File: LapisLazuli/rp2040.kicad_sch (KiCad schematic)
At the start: 32 parts, among them P1 USB_C_Plug_USB2.0, SW1 SW_Push, SW2 SW_Push, U10 W25Q128JVS, U11 RP2040, U9 NCP1117-3.3_SOT223, Y1 ABM8-272-T3

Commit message: Everything but I2C mux I think
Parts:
- removed U9: NCP1117-3.3_SOT223, Package_TO_SOT_SMD:SOT-223-3_TabPin2, symbol Regulator_Linear:NCP1117-3.3_SOT223
- added R19, R20: 5.1k, symbol Device:R_Small_US
- added U12: AZ1117IH-3.3TRG1, AZ1117IH-3.3TRG1:SOT230P700X185-4N, symbol AZ1117IH-3.3TRG1:AZ1117IH-3.3TRG1
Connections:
- net +3V3: now also U12.2 (OUTPUT), U12.4 (VOUT)
- net GND: now also R19.2, R20.2, U12.1 (GND)
- net USB_D+: now also P1.A6 (D+); no longer P1.A7 (D-)
- net USB_D-: now also P1.A7 (D-); no longer P1.A6 (D+)
- net VBUS: now also D1.1 (K), U12.3 (INPUT); no longer D1.2 (A)
- net at P1.A4 (VBUS), P1.A9 (VBUS), P1.B4 (VBUS)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: now also D1.2 (A); no longer D1.1 (K)
- net at P1.A5 (CC): now also R20.1
- net at P1.B5 (VCONN): now also R19.1
- net RS485_TX: now reaches U11.27 (GPIO16)
- net RS485_RX: now reaches U11.28 (GPIO17)
- net RS485_SEND: now reaches U11.29 (GPIO18)
- net I2C_SDA: now reaches U11.31 (GPIO20)
- net I2C_SCL: now reaches U11.32 (GPIO21)
- net I2C_MUX_RESET': now reaches U11.34 (GPIO22)
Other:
- moved on the sheet: C20, D1

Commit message: Most footprints and second I2C extender
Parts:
- C17, C18: footprint Capacitor_SMD:C_0402_1005Metric -> Capacitor_SMD:C_0603_1608Metric; Digikey (none) -> C1644; LCSC (none) -> C1644
- C19, C20, C33: Digikey (none) -> C19702; LCSC (none) -> C19702
- C21, C22, C23, C25, C27, C28, C29, C30, C31, C32: footprint Capacitor_SMD:C_0402_1005Metric -> Capacitor_SMD:C_0603_1608Metric; Digikey (none) -> C14663; LCSC (none) -> C14663
- C24, C26: footprint Capacitor_SMD:C_0402_1005Metric -> Capacitor_SMD:C_0603_1608Metric; Digikey (none) -> C15849; LCSC (none) -> C15849
- C34: value 0.1uF -> 100n; footprint Capacitor_SMD:C_0603_1608Metric_Pad1.08x0.95mm_HandSolder -> Capacitor_SMD:C_0603_1608Metric; Digikey (none) -> C14663; LCSC (none) -> C14663
- D1: Digikey (none) -> C191023; LCSC (none) -> C191023
- P1: footprint (none) -> Connector_USB:USB_C_Receptacle_HRO_TYPE-C-31-M-12; LCSC (none) -> C165948
- R13, R15: footprint Resistor_SMD:R_0402_1005Metric -> Resistor_SMD:R_0603_1608Metric; LCSC (none) -> C21190
- R14: footprint Resistor_SMD:R_0402_1005Metric -> Resistor_SMD:R_0603_1608Metric
- R16, R17: footprint Resistor_SMD:R_0402_1005Metric -> Resistor_SMD:R_0603_1608Metric; LCSC (none) -> C25190
- R18: footprint Resistor_SMD:R_0603_1608Metric_Pad0.98x0.95mm_HandSolder -> Resistor_SMD:R_0603_1608Metric; LCSC (none) -> C25804
- R19, R20: footprint (none) -> Resistor_SMD:R_0603_1608Metric; LCSC (none) -> C23186
- SW1, SW2: LCSC (none) -> C221784
- U10: LCSC (none) -> C97521
- U11: footprint RP2040_minimal_r2:RP2040-QFN-56 -> MCU_RaspberryPi_and_Boards:RP2040-QFN-56; Digikey (none) -> C2040; LCSC (none) -> C2040
- U12: footprint AZ1117IH-3.3TRG1:SOT230P700X185-4N -> Package_TO_SOT_SMD:SOT-223-3_TabPin2; LCSC (none) -> C108495
- Y1: Digikey (none) -> C20625731; LCSC (none) -> C20625731

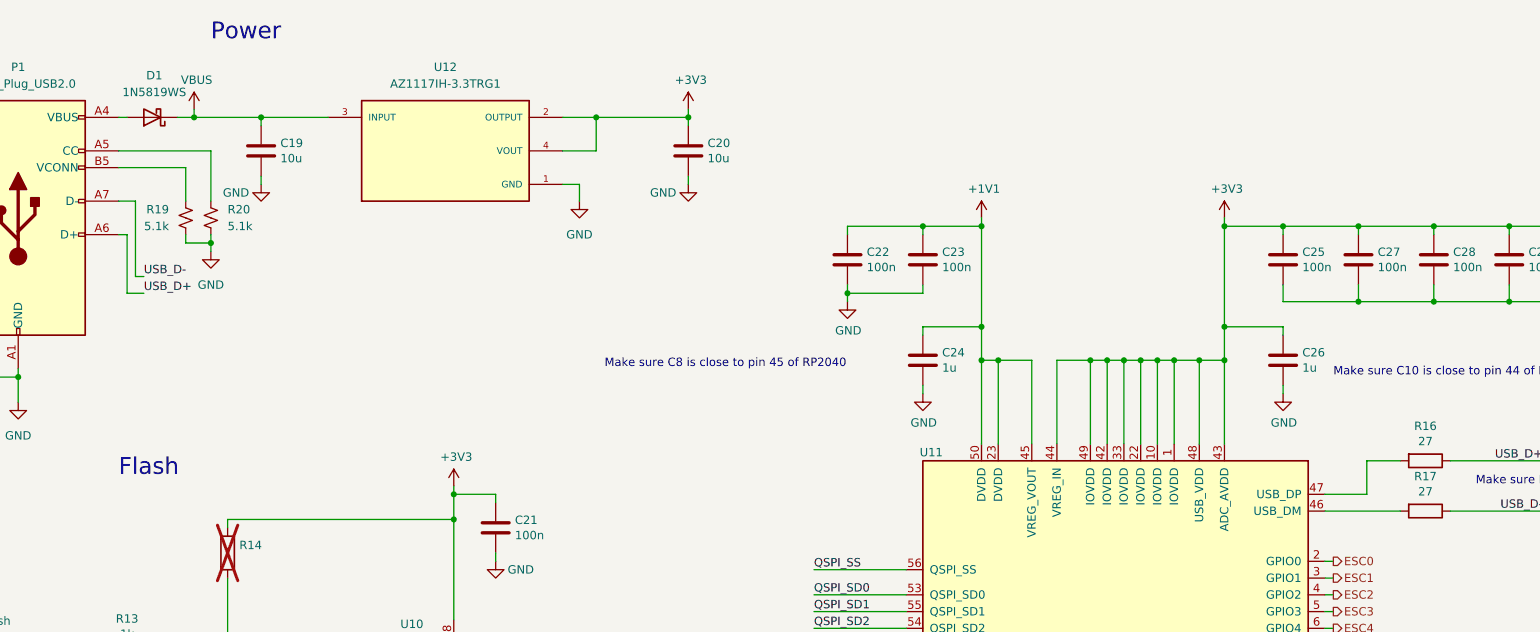
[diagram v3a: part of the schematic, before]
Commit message: Add current pcb layout
- Missing connections to power board
- Missing LEDs
- Missing Test Points
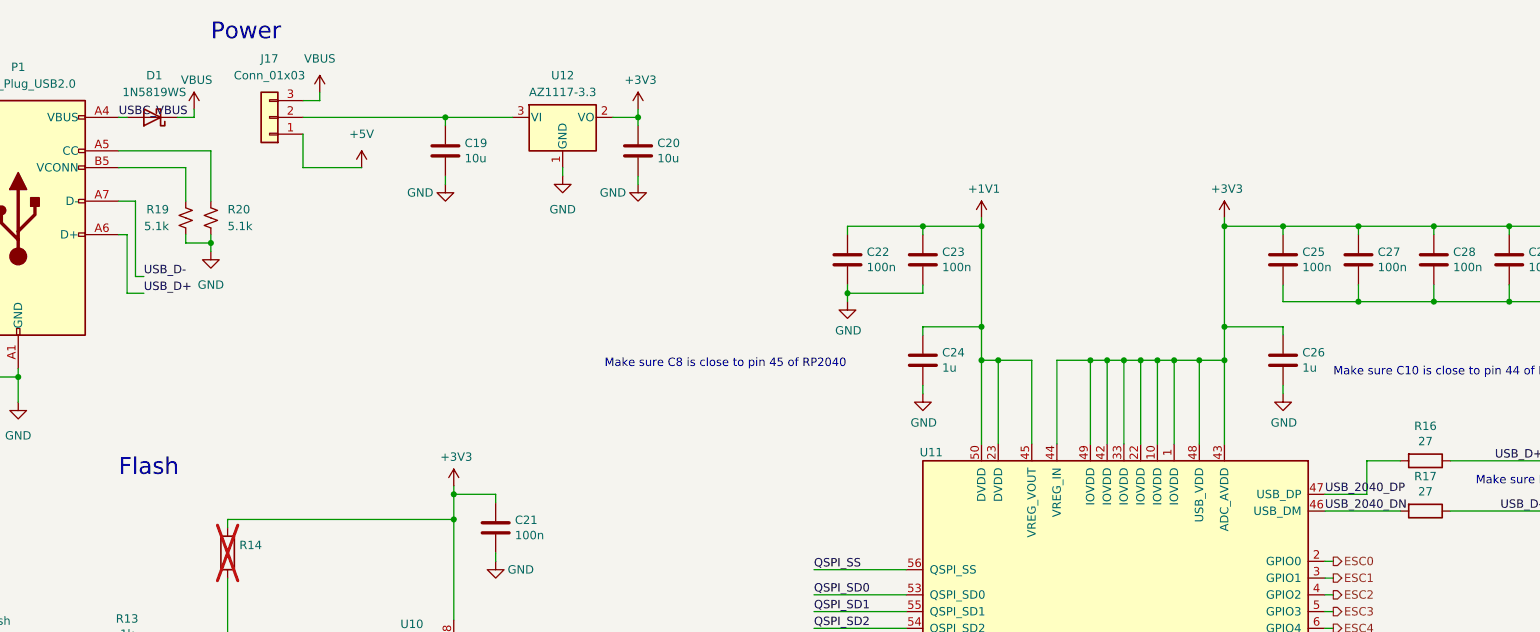
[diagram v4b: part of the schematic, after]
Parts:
- removed U12: AZ1117IH-3.3TRG1, Package_TO_SOT_SMD:SOT-223-3_TabPin2, symbol AZ1117IH-3.3TRG1:AZ1117IH-3.3TRG1
- added J17: Conn_01x03, Connector_PinHeader_2.54mm:PinHeader_1x03_P2.54mm_Vertical, symbol Connector_Generic:Conn_01x03
- added U12: AZ1117-3.3, Package_TO_SOT_SMD:SOT-223-3_TabPin2, symbol Regulator_Linear:AZ1117-3.3
- U10: footprint Package_SO:SOIC-8_5.23x5.23mm_P1.27mm -> footprints:SOIC127P790X216-8N
- U11: footprint MCU_RaspberryPi_and_Boards:RP2040-QFN-56 -> RP2040_minimal_r2:RP2040-QFN-56_SMALLER_VIAS
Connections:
- net +3V3: now also U12.2 (VO)
- net GND: now also U12.1 (GND)
- net VBUS: now also J17.3 (Pin_3); no longer C19.1
- net USBC_VBUS: now reaches D1.2 (A), P1.A4 (VBUS), P1.A9 (VBUS), P1.B4 (VBUS), P1.B9 (VBUS)
- net USB_2040_DN: now reaches R17.2, U11.46 (USB_DM)
- net USB_2040_DP: now reaches R16.2, U11.47 (USB_DP)
- new net: C19.1, J17.2 (Pin_2), U12.3 (VI)
- new net +5V: J17.1 (Pin_1)
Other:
- moved on the sheet: C19, C20
